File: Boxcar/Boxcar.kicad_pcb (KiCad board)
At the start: 2 copper layers, 47.5 x 16.5 mm, 0 parts

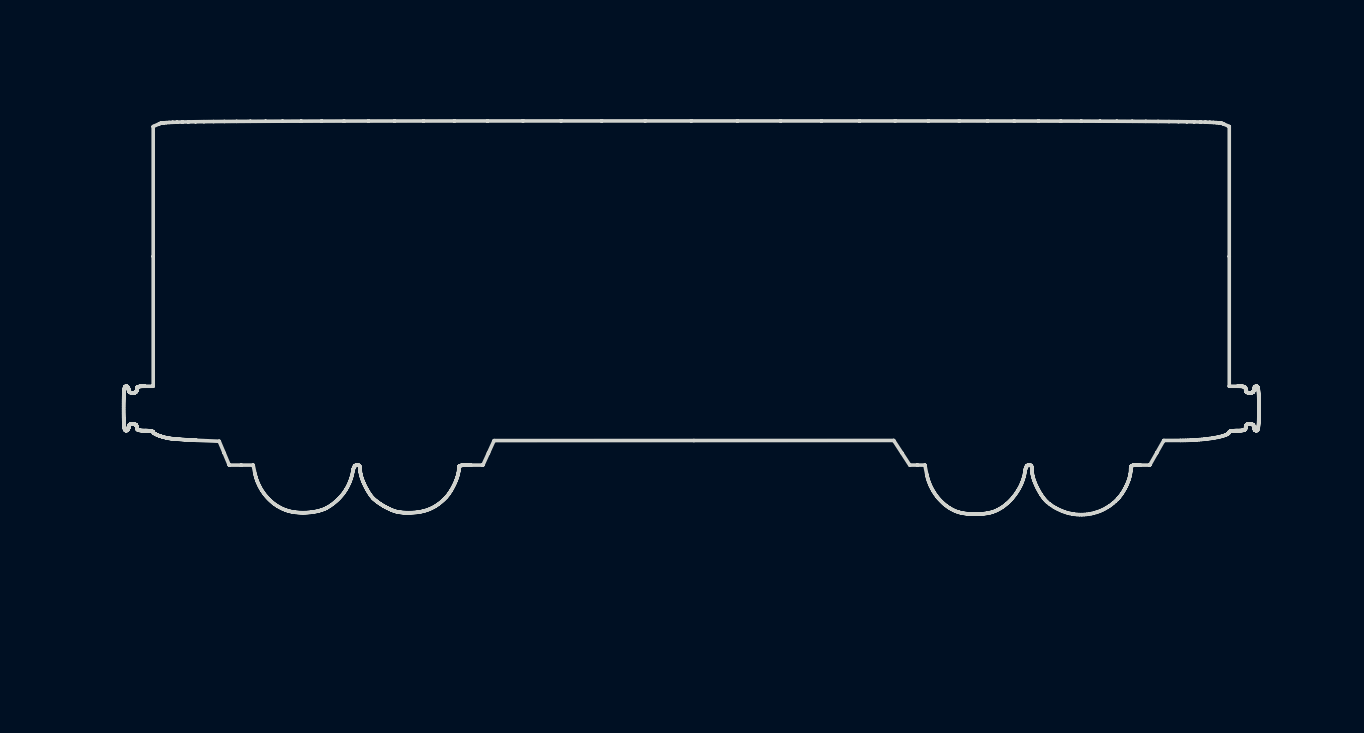
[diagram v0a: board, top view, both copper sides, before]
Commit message: Add & Align Pins
Add pins to all trains and set proper locations
Move RGB LEDs and resistors
Connect RGB LEDs to resistors and speaker to Arduino
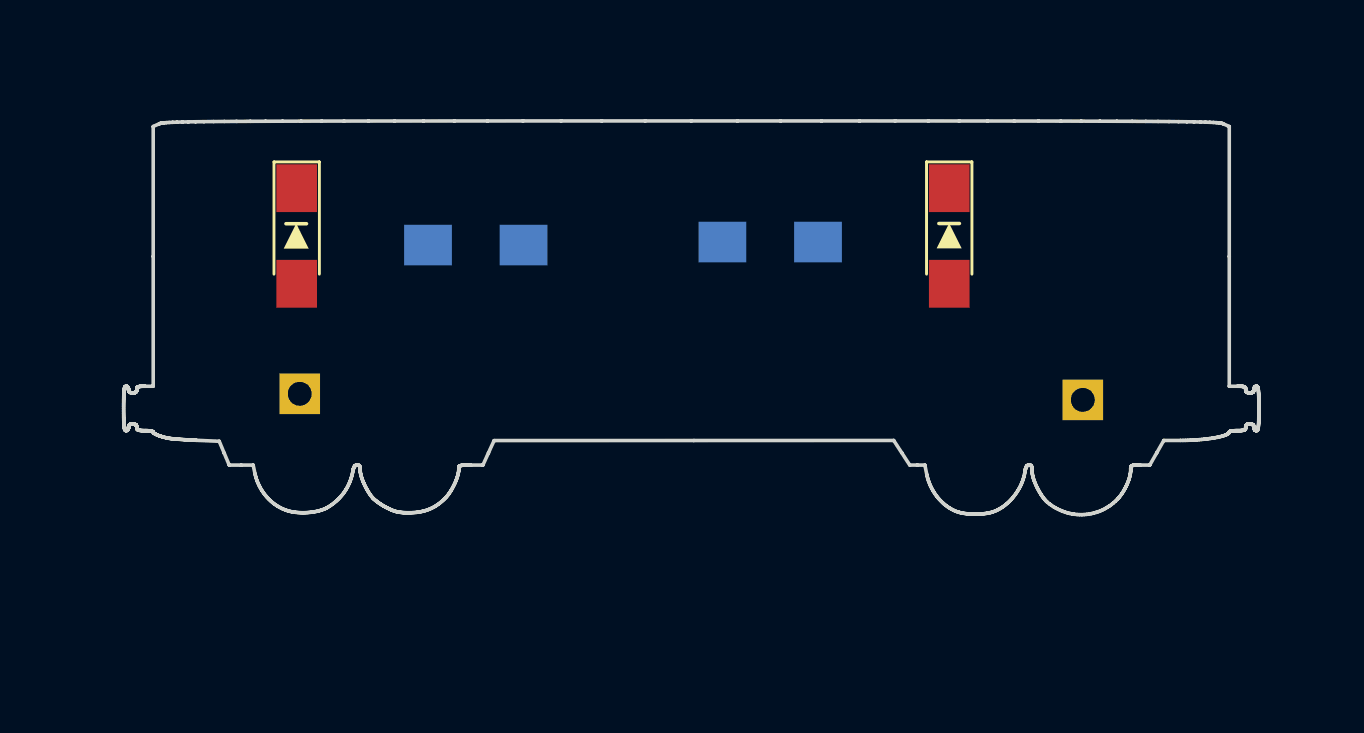
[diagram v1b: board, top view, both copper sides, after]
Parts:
- added D1: LED, LEDs:LED_1206_HandSoldering, F.Cu at (7.24, 54.1)
- added D2: LED, LEDs:LED_1206_HandSoldering, F.Cu at (34.5, 54.1)
- added MK1: VCC, Pin_Headers:Pin_Header_Angled_1x01_Pitch2.54mm, B.Cu at (7.37, 60.7)
- added MK2: GND, Pin_Headers:Pin_Header_Angled_1x01_Pitch2.54mm, B.Cu at (40.1, 61.0)
- added R1: R, Resistors_SMD:R_1206_HandSoldering, B.Cu at (14.7, 54.5)
- added R2: R, Resistors_SMD:R_1206_HandSoldering, B.Cu at (27.1, 54.4)
- added REF**: LED_1206, Markings:LED_1206, F.Cu at (34.5, 54.0)
- added REF**: LED_1206, Markings:LED_1206, F.Cu at (7.22, 54.0)

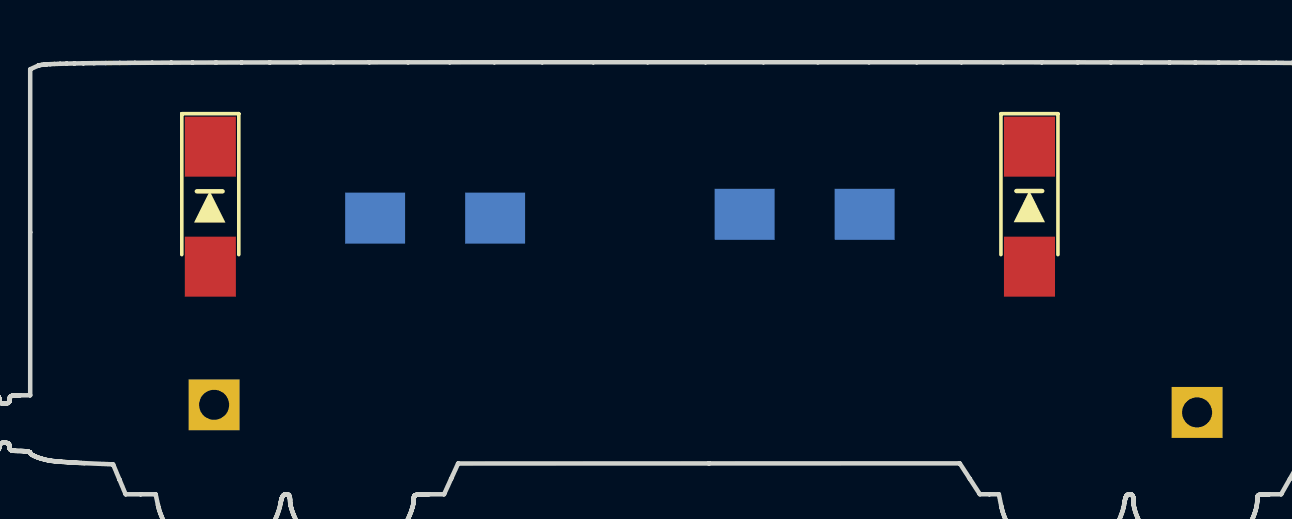
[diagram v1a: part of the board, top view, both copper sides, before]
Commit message: Change Schematic For RGB LEDs
Add transistors to control 3 RGB LEDs
Add Silkscreen detail to caboose
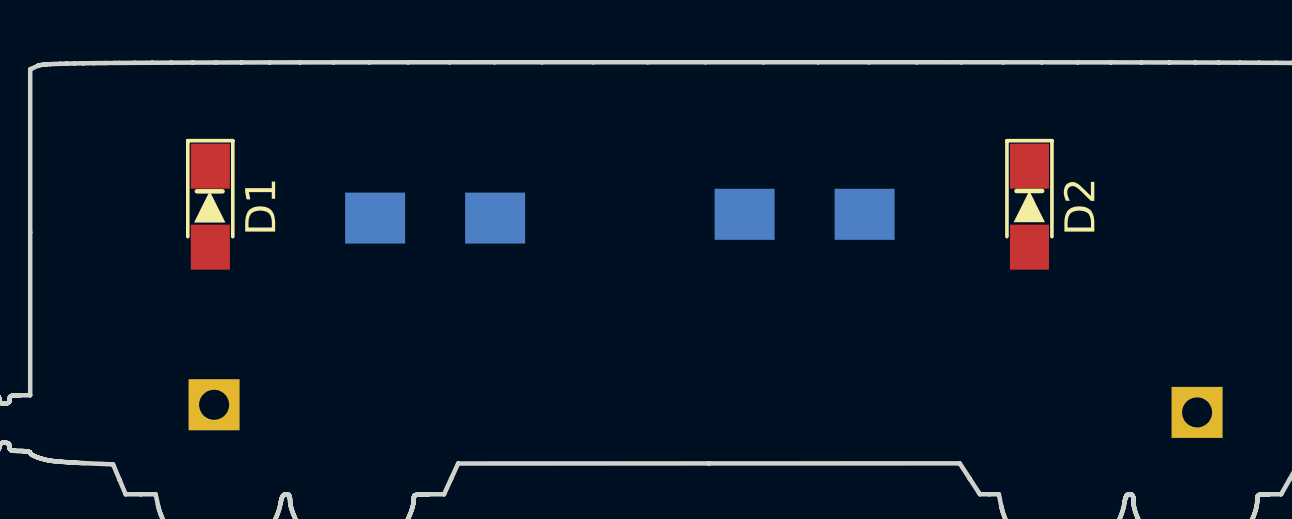
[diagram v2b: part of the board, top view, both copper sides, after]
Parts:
- D1, D2: footprint LEDs:LED_1206_HandSoldering -> LEDs:LED_0805_HandSoldering
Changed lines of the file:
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@@
-(kicad_pcb (version 20171130) (host pcbnew 5.0.0-rc2-dev-unknown-bf135b0~64~ubuntu16.04.1)
+(kicad_pcb (version 20171130) (host pcbnew 5.0.0-rc2-dev-unknown-d41e64b~65~ubuntu16.04.1)
   (general
     (thickness 1.6)
@@
     (fp_line (start -0.43 -0.43) (end 0.43 -0.43) (layer F.SilkS) (width 0.15))
   )
-  (module LEDs:LED_1206_HandSoldering (layer F.Cu)
-    (at 7.239 54.102 270)
-    (descr "LED SMD 1206, hand soldering")
-    (tags "LED 1206")
-    (attr smd)
-    (fp_text reference D1 (at 0 -1.85 270) (layer F.Fab)
-      (effects (font (size 1 1) (thickness 0.15)))
-    )
-    (fp_text value LED (at 0 1.9 270) (layer F.Fab)
-      (effects (font (size 1 1) (thickness 0.15)))
-    )
-    (fp_line (start 3.25 1.1) (end -3.25 1.1) (layer F.CrtYd) (width 0.05))
-    (fp_line (start 3.25 1.1) (end 3.25 -1.11) (layer F.CrtYd) (width 0.05))
-    (fp_line (start -3.25 -1.11) (end -3.25 1.1) (layer F.CrtYd) (width 0.05))
-    (fp_line (start -3.25 -1.11) (end 3.25 -1.11) (layer F.CrtYd) (width 0.05))
-    (fp_line (start -3.1 -0.95) (end 1.6 -0.95) (layer F.SilkS) (width 0.12))
-    (fp_line (start -3.1 0.95) (end 1.6 0.95) (layer F.SilkS) (width 0.12))
-    (fp_line (start -1.6 -0.8) (end 1.6 -0.8) (layer F.Fab) (width 0.1))
-    (fp_line (start 1.6 -0.8) (end 1.6 0.8) (layer F.Fab) (width 0.1))
-    (fp_line (start 1.6 0.8) (end -1.6 0.8) (layer F.Fab) (width 0.1))
-    (fp_line (start -1.6 0.8) (end -1.6 -0.8) (layer F.Fab) (width 0.1))
-    (fp_line (start -0.45 -0.4) (end -0.45 0.4) (layer F.Fab) (width 0.1))
-    (fp_line (start 0.2 0.4) (end -0.4 0) (layer F.Fab) (width 0.1))
-    (fp_line (start 0.2 -0.4) (end 0.2 0.4) (layer F.Fab) (width 0.1))
-    (fp_line (start -0.4 0) (end 0.2 -0.4) (layer F.Fab) (width 0.1))
-    (fp_line (start -3.1 -0.95) (end -3.1 0.95) (layer F.SilkS) (width 0.12))
-    (pad 2 smd rect (at 2 0 270) (size 2 1.7) (layers F.Cu F.Paste F.Mask)
-      (net 1 "Net-(D1-Pad2)"))
-    (pad 1 smd rect (at -2 0 270) (size 2 1.7) (layers F.Cu F.Paste F.Mask)
-      (net 2 /GND))
-    (model ${KISYS3DMOD}/LEDs.3dshapes/LED_1206.wrl
-      (at (xyz 0 0 0))
-      (scale (xyz 1 1 1))
-      (rotate (xyz 0 0 180))
-    )
-  )
-  (module LEDs:LED_1206_HandSoldering (layer F.Cu)
-    (at 34.544 54.102 270)
-    (descr "LED SMD 1206, hand soldering")
-    (tags "LED 1206")
-    (attr smd)
-    (fp_text reference D2 (at 0 -1.85 270) (layer F.Fab)
-      (effects (font (size 1 1) (thickness 0.15)))
-    )
-    (fp_text value LED (at 0 1.9 270) (layer F.Fab)
-      (effects (font (size 1 1) (thickness 0.15)))
-    )
-    (fp_line (start -3.1 -0.95) (end -3.1 0.95) (layer F.SilkS) (width 0.12))
-    (fp_line (start -0.4 0) (end 0.2 -0.4) (layer F.Fab) (width 0.1))
-    (fp_line (start 0.2 -0.4) (end 0.2 0.4) (layer F.Fab) (width 0.1))
-    (fp_line (start 0.2 0.4) (end -0.4 0) (layer F.Fab) (width 0.1))
-    (fp_line (start -0.45 -0.4) (end -0.45 0.4) (layer F.Fab) (width 0.1))
-    (fp_line (start -1.6 0.8) (end -1.6 -0.8) (layer F.Fab) (width 0.1))
-    (fp_line (start 1.6 0.8) (end -1.6 0.8) (layer F.Fab) (width 0.1))
-    (fp_line (start 1.6 -0.8) (end 1.6 0.8) (layer F.Fab) (width 0.1))
-    (fp_line (start -1.6 -0.8) (end 1.6 -0.8) (layer F.Fab) (width 0.1))
-    (fp_line (start -3.1 0.95) (end 1.6 0.95) (layer F.SilkS) (width 0.12))
-    (fp_line (start -3.1 -0.95) (end 1.6 -0.95) (layer F.SilkS) (width 0.12))
-    (fp_line (start -3.25 -1.11) (end 3.25 -1.11) (layer F.CrtYd) (width 0.05))
-    (fp_line (start -3.25 -1.11) (end -3.25 1.1) (layer F.CrtYd) (width 0.05))
-    (fp_line (start 3.25 1.1) (end 3.25 -1.11) (layer F.CrtYd) (width 0.05))
-    (fp_line (start 3.25 1.1) (end -3.25 1.1) (layer F.CrtYd) (width 0.05))
-    (pad 1 smd rect (at -2 0 270) (size 2 1.7) (layers F.Cu F.Paste F.Mask)
-      (net 2 /GND))
-    (pad 2 smd rect (at 2 0 270) (size 2 1.7) (layers F.Cu F.Paste F.Mask)
-      (net 3 "Net-(D2-Pad2)"))
-    (model ${KISYS3DMOD}/LEDs.3dshapes/LED_1206.wrl
-      (at (xyz 0 0 0))
-      (scale (xyz 1 1 1))
-      (rotate (xyz 0 0 180))
-    )
-  )
   (module Pin_Headers:Pin_Header_Angled_1x01_Pitch2.54mm (layer B.Cu)
     (at 7.366 60.706 270)
@@
     )
   )
+  (module LEDs:LED_0805_HandSoldering (layer F.Cu)
+    (at 7.239 54.102 270)
+    (descr "Resistor SMD 0805, hand soldering")
+    (tags "resistor 0805")
+    (attr smd)
+    (fp_text reference D1 (at 0 -1.7 270) (layer F.SilkS)
+      (effects (font (size 1 1) (thickness 0.15)))
+    )
+    (fp_text value LED (at 0 1.75 270) (layer F.Fab)
+      (effects (font (size 1 1) (thickness 0.15)))
+    )
+    (fp_line (start -2.2 -0.75) (end -2.2 0.75) (layer F.SilkS) (width 0.12))
+    (fp_line (start 2.35 0.9) (end -2.35 0.9) (layer F.CrtYd) (width 0.05))
+    (fp_line (start 2.35 0.9) (end 2.35 -0.9) (layer F.CrtYd) (width 0.05))
+    (fp_line (start -2.35 -0.9) (end -2.35 0.9) (layer F.CrtYd) (width 0.05))
+    (fp_line (start -2.35 -0.9) (end 2.35 -0.9) (layer F.CrtYd) (width 0.05))
+    (fp_line (start -2.2 -0.75) (end 1 -0.75) (layer F.SilkS) (width 0.12))
+    (fp_line (start 1 0.75) (end -2.2 0.75) (layer F.SilkS) (width 0.12))
+    (fp_line (start -1 -0.62) (end 1 -0.62) (layer F.Fab) (width 0.1))
+    (fp_line (start 1 -0.62) (end 1 0.62) (layer F.Fab) (width 0.1))
+    (fp_line (start 1 0.62) (end -1 0.62) (layer F.Fab) (width 0.1))
+    (fp_line (start -1 0.62) (end -1 -0.62) (layer F.Fab) (width 0.1))
+    (fp_line (start 0.2 -0.4) (end 0.2 0.4) (layer F.Fab) (width 0.1))
+    (fp_line (start 0.2 0.4) (end -0.4 0) (layer F.Fab) (width 0.1))
+    (fp_line (start -0.4 0) (end 0.2 -0.4) (layer F.Fab) (width 0.1))
+    (fp_line (start -0.4 -0.4) (end -0.4 0.4) (layer F.Fab) (width 0.1))
+    (pad 2 smd rect (at 1.35 0 270) (size 1.5 1.3) (layers F.Cu F.Paste F.Mask)
+      (net 1 "Net-(D1-Pad2)"))
+    (pad 1 smd rect (at -1.35 0 270) (size 1.5 1.3) (layers F.Cu F.Paste F.Mask)
+      (net 2 /GND))
+    (model ${KISYS3DMOD}/LEDs.3dshapes/LED_0805.wrl
+      (at (xyz 0 0 0))
+      (scale (xyz 1 1 1))
+      (rotate (xyz 0 0 0))
+    )
+  )
+  (module LEDs:LED_0805_HandSoldering (layer F.Cu)
+    (at 34.544 54.102 270)
+    (descr "Resistor SMD 0805, hand soldering")
+    (tags "resistor 0805")
+    (attr smd)
+    (fp_text reference D2 (at 0 -1.7 270) (layer F.SilkS)
+      (effects (font (size 1 1) (thickness 0.15)))
+    )
+    (fp_text value LED (at 0 1.75 270) (layer F.Fab)
+      (effects (font (size 1 1) (thickness 0.15)))
+    )
+    (fp_line (start -0.4 -0.4) (end -0.4 0.4) (layer F.Fab) (width 0.1))
+    (fp_line (start -0.4 0) (end 0.2 -0.4) (layer F.Fab) (width 0.1))
+    (fp_line (start 0.2 0.4) (end -0.4 0) (layer F.Fab) (width 0.1))
+    (fp_line (start 0.2 -0.4) (end 0.2 0.4) (layer F.Fab) (width 0.1))
+    (fp_line (start -1 0.62) (end -1 -0.62) (layer F.Fab) (width 0.1))
+    (fp_line (start 1 0.62) (end -1 0.62) (layer F.Fab) (width 0.1))
+    (fp_line (start 1 -0.62) (end 1 0.62) (layer F.Fab) (width 0.1))
+    (fp_line (start -1 -0.62) (end 1 -0.62) (layer F.Fab) (width 0.1))
+    (fp_line (start 1 0.75) (end -2.2 0.75) (layer F.SilkS) (width 0.12))
+    (fp_line (start -2.2 -0.75) (end 1 -0.75) (layer F.SilkS) (width 0.12))
+    (fp_line (start -2.35 -0.9) (end 2.35 -0.9) (layer F.CrtYd) (width 0.05))
+    (fp_line (start -2.35 -0.9) (end -2.35 0.9) (layer F.CrtYd) (width 0.05))
+    (fp_line (start 2.35 0.9) (end 2.35 -0.9) (layer F.CrtYd) (width 0.05))
+    (fp_line (start 2.35 0.9) (end -2.35 0.9) (layer F.CrtYd) (width 0.05))
+    (fp_line (start -2.2 -0.75) (end -2.2 0.75) (layer F.SilkS) (width 0.12))
+    (pad 1 smd rect (at -1.35 0 270) (size 1.5 1.3) (layers F.Cu F.Paste F.Mask)
+      (net 2 /GND))
+    (pad 2 smd rect (at 1.35 0 270) (size 1.5 1.3) (layers F.Cu F.Paste F.Mask)
+      (net 3 "Net-(D2-Pad2)"))
+    (model ${KISYS3DMOD}/LEDs.3dshapes/LED_0805.wrl
+      (at (xyz 0 0 0))
+      (scale (xyz 1 1 1))
+      (rotate (xyz 0 0 0))
+    )
+  )

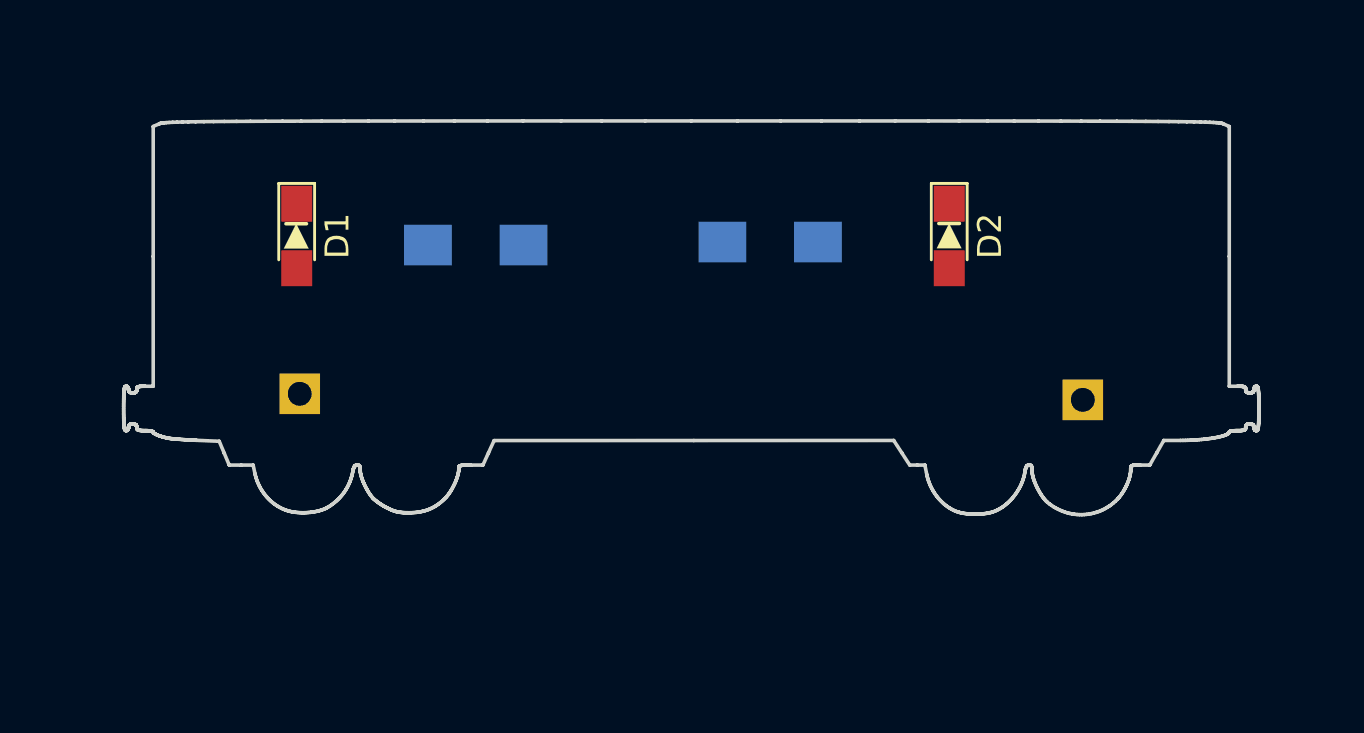
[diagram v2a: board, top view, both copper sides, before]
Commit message: Finalize Tracks
Finish tracks for 3 RGB LEDs
Move date to locomotive, remove from caboose
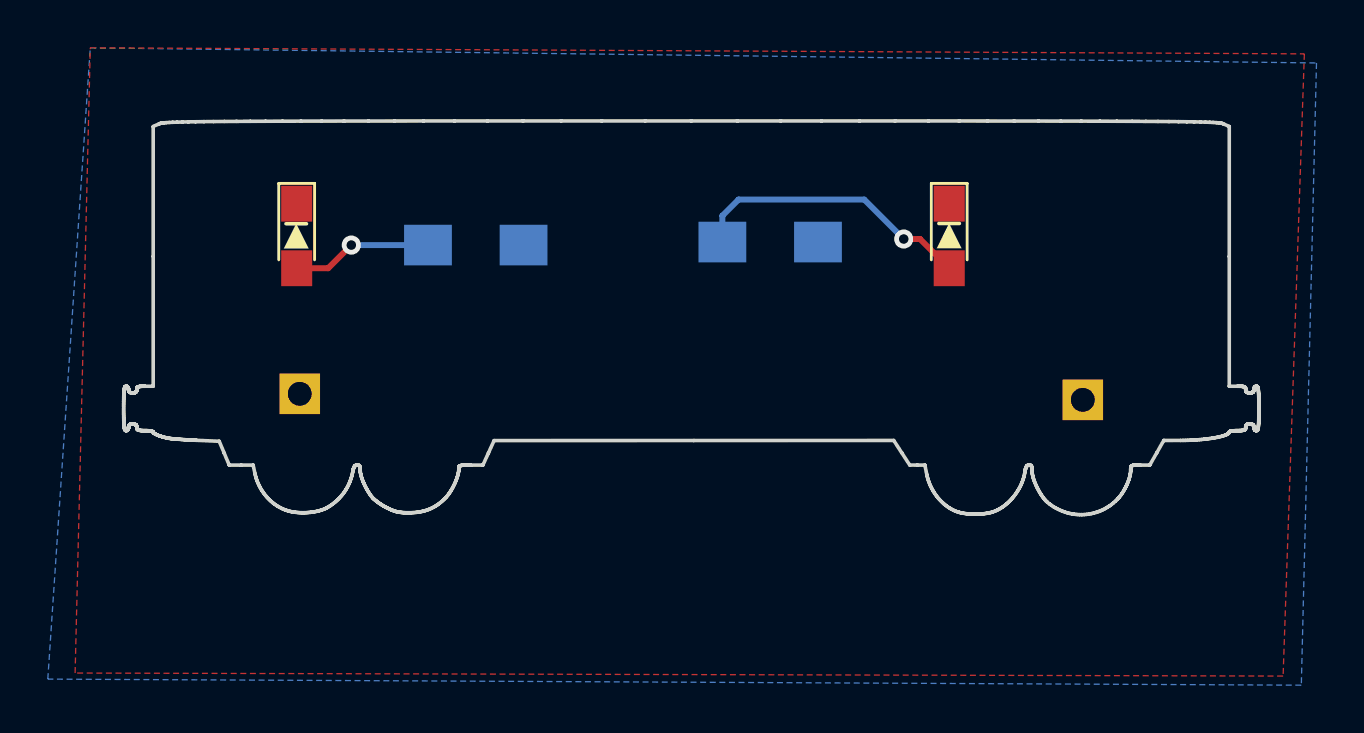
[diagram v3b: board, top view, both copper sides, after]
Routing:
- net Net-(D2-Pad2): track 0.00 -> 12.1 mm, vias 0 -> 1
- net Net-(D1-Pad2): track 0.00 -> 5.89 mm, vias 0 -> 1
- added copper zone on F.Cu, net /GND
- added copper zone on B.Cu, net /VCC
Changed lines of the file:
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@@
-(kicad_pcb (version 20171130) (host pcbnew 5.0.0-rc2-dev-unknown-d41e64b~65~ubuntu16.04.1)
+(kicad_pcb (version 20171130) (host pcbnew 5.0.0-rc2-dev-unknown-2bab30d~65~ubuntu16.04.1)
   (general
     (thickness 1.6)
     (drawings 1486)
-    (tracks 0)
+    (tracks 11)
     (zones 0)
     (modules 8)
@@
     (tags "resistor 0805")
     (attr smd)
-    (fp_text reference D1 (at 0 -1.7 270) (layer F.SilkS)
+    (fp_text reference D1 (at 0 -1.7 270) (layer F.Fab)
       (effects (font (size 1 1) (thickness 0.15)))
     )
@@
     (tags "resistor 0805")
     (attr smd)
-    (fp_text reference D2 (at 0 -1.7 270) (layer F.SilkS)
+    (fp_text reference D2 (at 0 -1.7 270) (layer F.Fab)
       (effects (font (size 1 1) (thickness 0.15)))
     )
@@
   (gr_line (start 0.623632 62.22694) (end 0.613255 62.223533) (layer Edge.Cuts) (width 0.15))
   (gr_line (start 0.635 62.23) (end 0.623632 62.22694) (layer Edge.Cuts) (width 0.15))
+  (via (at 9.525 54.483) (size 0.8) (drill 0.4) (layers F.Cu B.Cu) (net 1))
+  (segment (start 12.732 54.483) (end 9.525 54.483) (width 0.25) (layer B.Cu) (net 1))
+  (segment (start 8.556 55.452) (end 7.239 55.452) (width 0.25) (layer F.Cu) (net 1))
+  (segment (start 9.525 54.483) (end 8.556 55.452) (width 0.25) (layer F.Cu) (net 1))
+  (segment (start 25.051 53.256) (end 25.729 52.578) (width 0.25) (layer B.Cu) (net 3))
+  (segment (start 25.051 54.356) (end 25.051 53.256) (width 0.25) (layer B.Cu) (net 3))
+  (via (at 32.639 54.229) (size 0.8) (drill 0.4) (layers F.Cu B.Cu) (net 3))
+  (segment (start 30.988 52.578) (end 32.639 54.229) (width 0.25) (layer B.Cu) (net 3))
+  (segment (start 25.729 52.578) (end 30.988 52.578) (width 0.25) (layer B.Cu) (net 3))
+  (segment (start 33.321 54.229) (end 34.544 55.452) (width 0.25) (layer F.Cu) (net 3))
+  (segment (start 32.639 54.229) (end 33.321 54.229) (width 0.25) (layer F.Cu) (net 3))
+  (zone (net 2) (net_name /GND) (layer F.Cu) (hatch edge 0.508)
+    (connect_pads (clearance 0.508))
+    (min_thickness 0.254)
+    (fill yes (arc_segments 16) (thermal_gap 0.508) (thermal_bridge_width 0.508))
+    (polygon
+      (pts
+        (xy -1.397 46.228) (xy 49.403 46.482) (xy 48.514 72.517) (xy -2.032 72.39)
+      )
+    )
+  )
+  (zone (net 4) (net_name /VCC) (layer B.Cu) (hatch edge 0.508)
+    (connect_pads (clearance 0.508))
+    (min_thickness 0.254)
+    (fill yes (arc_segments 16) (thermal_gap 0.508) (thermal_bridge_width 0.508))
+    (polygon
+      (pts
+        (xy -1.397 46.228) (xy 49.911 46.863) (xy 49.276 72.898) (xy -3.175 72.644)
+      )
+    )
+  )
 )
